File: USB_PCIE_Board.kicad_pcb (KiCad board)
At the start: 4 copper layers, 98.2 x 111.5 mm, 175 parts, among them J1 Bus_PCI_Express_x1, J2 0484050001, J3 0484050001, J4 0484050001, J5 0484050001, Q1 2SA1576AT106R, Q2 2SC4081T106R, Q4 DMT6016LSS-13, Q5 SI4134DY-T1-GE3, U1 UPD720201K8-711-BAC-A, U10 AP2191SG-13, U11 AP2191SG-13, U12 SP3011-06UTG, U13 SP3011-06UTG, U14 SP3011-06UTG, U15 SP3011-06UTG, U2 MX25L4006EM1I-12G, U3 LM22678TJ-5.0/NOPB, U4 LTC3872ETS8-TRPBF, U5 RT5762CHGH6F, U6 641737-1, U7 AP7215-33YG-13, U8 AP2191SG-13, U9 AP2191SG-13, X1 CS14522-24M

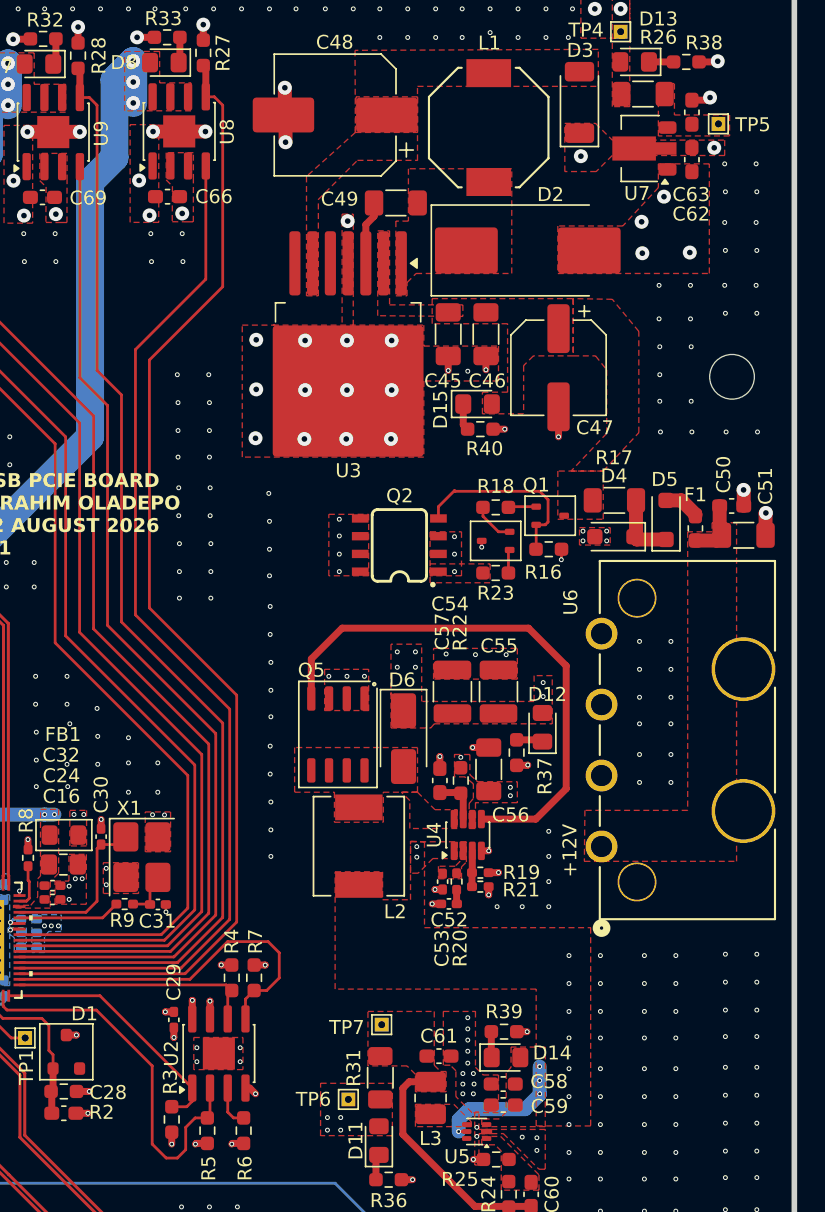
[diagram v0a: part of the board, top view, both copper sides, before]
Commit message: Correct U1 part number to UPD720201K8-701-BAC-A; fix silkscreen; add LCSC order BOM
Schematic symbol/value/datasheet now match the part actually ordered and
populated. Regenerated schematic PDF and added the final LCSC BOM CSV.

Co-Authored-By: Claude Sonnet 5 <noreply@anthropic.com>
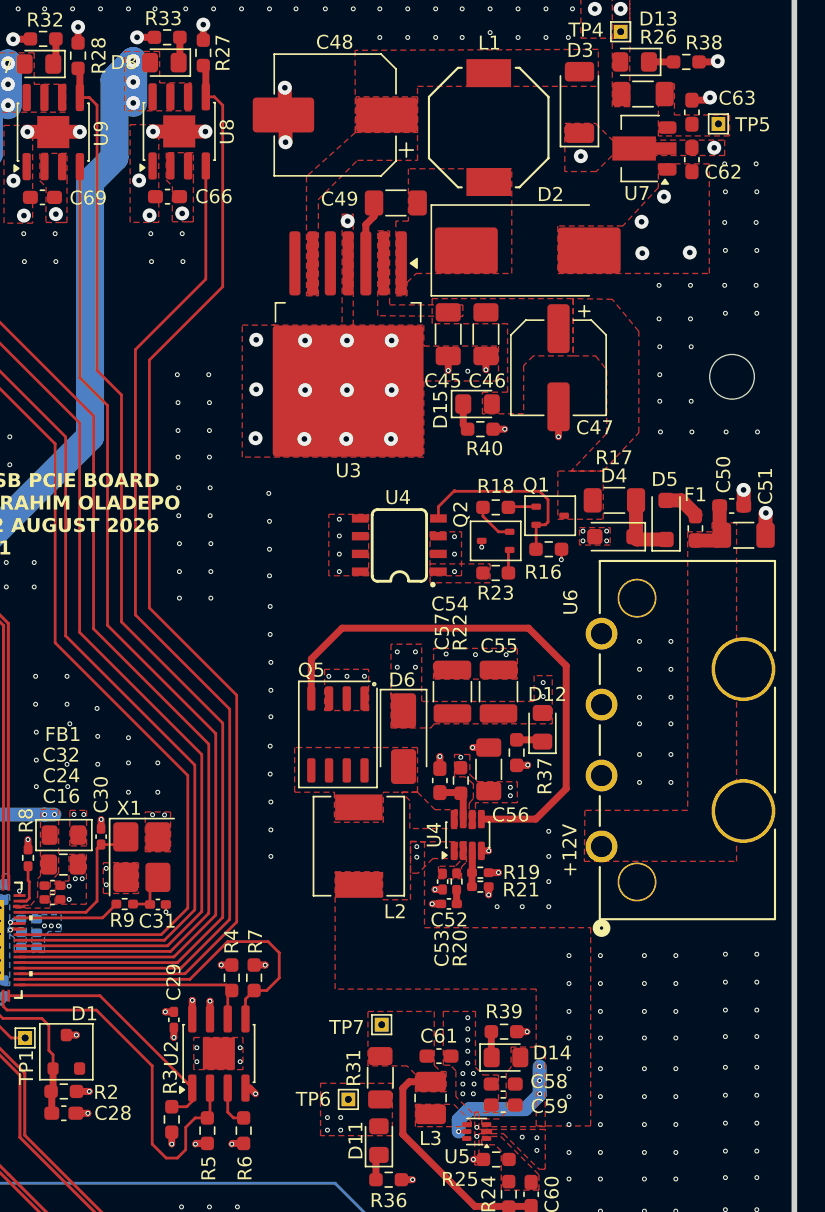
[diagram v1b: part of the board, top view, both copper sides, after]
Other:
- board text added: "U4"
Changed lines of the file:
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@@
 		(tags "capacitor handsolder")
 		(property "Reference" "C63"
-			(at -5.9 -0.05 0)
+			(at 1 3.25 0)
 			(layer "F.SilkS")
 			(effects
@@
 		(tags "capacitor handsolder")
 		(property "Reference" "C62"
-			(at 3.9 0.05 0)
+			(at 0.9 -2.25 0)
 			(layer "F.SilkS")
 			(effects
@@
 		(tags "resistor handsolder")
 		(property "Reference" "R2"
-			(at -2.71 -1.5 0)
+			(at -3.03 -0.07 0)
 			(layer "F.SilkS")
 			(effects
@@
 		(tags "capacitor handsolder")
 		(property "Reference" "C28"
-			(at 3.18 -1.48 0)
+			(at 3.53 0.01 0)
 			(layer "F.SilkS")
 			(effects
@@
 		(tags "SOT-323 SC-70")
 		(property "Reference" "Q2"
-			(at 6.875 3.225 180)
+			(at 2.5 1.9 270)
 			(layer "F.SilkS")
 			(effects
@@
 		)
 	)
+	(gr_text "U4"
+		(at 121.3 74.6 0)
+		(layer "F.SilkS")
+		(effects
+			(font
+				(size 1 1)
+				(thickness 0.15)
+			)
+		)
+	)
